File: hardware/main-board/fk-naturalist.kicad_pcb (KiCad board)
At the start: 2 copper layers, 103 x 37.5 mm, 124 parts, among them J1 RF-SMA-EDGE, J10 S2B-PH-SM4-TB, J11 RF-SMA-EDGE, J12 Conn_01x02, J13 CONN_01x06, J14 Conn_01x02, J2 Conn_01x02, J3 S2B-PH-SM4-TB, J4 Conn_01x01, J5 CONN_01x03_SERIAL, J6 Conn_01x05, J7 CONN_02x05_SWD, J8 CONN_01x02, J9 MICRO-USB, M10 FIDUCIAL, M11 FIDUCIAL, M2 FIDUCIAL, M5 FIDUCIAL, M7 MICROSD, M8 FIDUCIAL, M9 FIDUCIAL, Q1 2N7002LT1G, SW1 SPNO, SW2 SPNO, U1 ATWINC1500-MR210PA, U10 FGPMMOPA6H, U11 MAX1704XX, U12 TPS2052B, U13 SK6812, U14 MCP1700T-3302E/MB, U2 ATSAMD21G18A-AU, U3 RFM95W, U4 24AA02E64, U5 S25FL116K0XMFI041, U6 BQ24074RGTT, U7 PCF8523, U8 TL5209, U9 TL5209, Y1 FC-135, Y2 FC-135

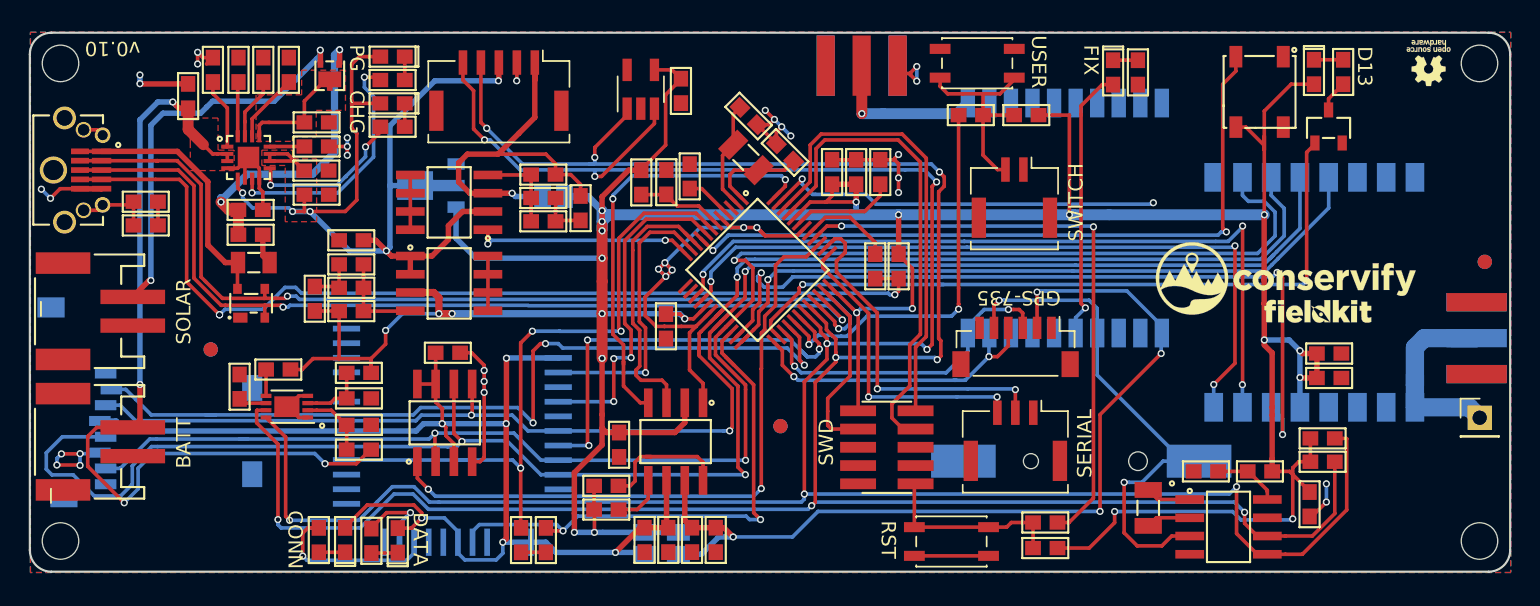
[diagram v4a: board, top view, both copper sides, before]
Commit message: Add new 9 pin sensor connector.
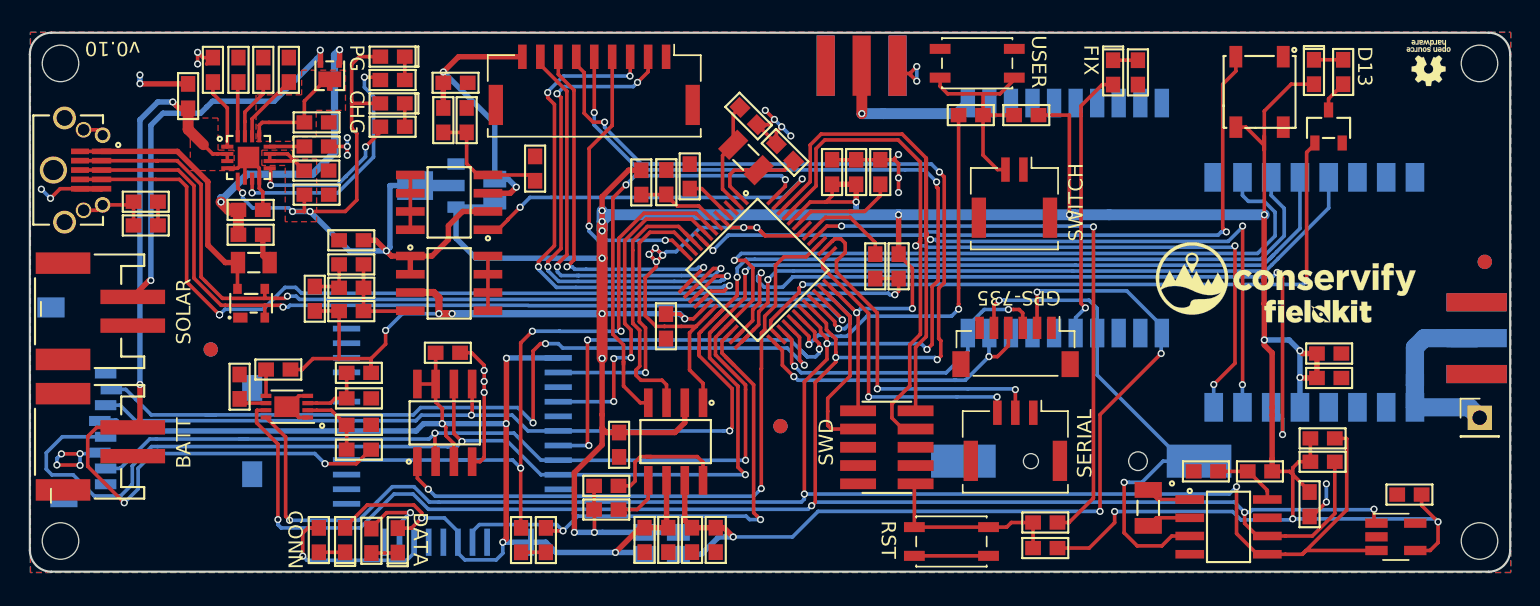
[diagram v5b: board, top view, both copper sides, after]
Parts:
- J6: value Conn_01x05 -> CONN_01x09; footprint conservify:Molex_CLIK-Mate_502382-0570_1x05_P1.25mm_Vertical -> conservify:Molex_CLIK-Mate_502382-0970_1x09_P1.25mm_Vertical
- moved U4 61.1 mm to (169.0, 144.1), turned to 0 degrees
- moved C11 57.9 mm to (170.0, 141.1), turned to 180 degrees
- moved C30 12.3 mm to (103.6, 112.5), turned to 0 degrees
- moved R13 7.92 mm to (102.8, 115.1), turned to 270 degrees
- moved C29 7.60 mm to (104.4, 115.1), turned to 90 degrees
- moved J6 6.65 mm to (113.3, 112.6)
- moved J14 4.11 mm to (106.3, 120.0), turned to 270 degrees
- moved R14 3.71 mm to (109.2, 118.5), turned to 90 degrees
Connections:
- J6 pad 1: /MODULE_3V3 -> GND
- J6 pad 2: GND -> /I2S_BCLK
- J6 pad 3: VBUS -> /I2S_WS
- J6 pad 4: /SCL -> /I2S_DATA
- J7 pad 2: /SWDIO -> /D1_RADIO_D1
- J7 pad 4: /SWCLK -> /D0_RADIO_D2
- U2 pad 12: /D9_MODULE_EN -> /I2S_DATA
- U2 pad 15: /D1_RADIO_D1 -> /I2S_BCLK
- U2 pad 16: /D0_RADIO_D2 -> /I2S_WS
- U2 pad 45: /SWCLK -> /D0_RADIO_D2
- U2 pad 46: /SWDIO -> /D1_RADIO_D1
- U2 pad 47: /A5 -> /D9_MODULE_EN
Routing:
- net /I2S_WS: track 0.00 -> 36.9 mm, vias 0 -> 4
- net /I2S_BCLK: track 0.00 -> 36.6 mm, vias 0 -> 4
- net /SWCLK: track 34.0 -> 0.00 mm
- net /SWDIO: track 32.1 -> 0.00 mm
- net /SCL2: track 0.00 -> 30.6 mm, vias 0 -> 2
- net /A5: track 27.7 -> 0.00 mm, vias 2 -> 0
- net /SDA2: track 0.00 -> 26.7 mm, vias 0 -> 2
- net /I2S_DATA: track 0.00 -> 20.2 mm, vias 0 -> 2
- net /D1_RADIO_D1: track 53.4 -> 73.1 mm
- net /D0_RADIO_D2: track 51.4 -> 68.9 mm
- net VBUS: track 74.1 -> 59.8 mm, vias 5 -> 4
- net /D9_MODULE_EN: track 15.2 -> 25.7 mm
- net /SDA: track 173.3 -> 163.0 mm, vias 8 -> 7
- net 3V3: track 275.5 -> 281.6 mm, vias 23 -> 24
- net /MODULE_3V3: track 27.1 -> 22.0 mm, vias 1 -> 2
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
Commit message: Use more compatible FP for flash.
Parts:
- U5: footprint conservify:SOIC-8-N -> conservify:SOIC-8-N-WIDE
- moved C18 1.10 mm to (103.1, 130.2)
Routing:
- net /D26_FLASH_CS: track 45.5 -> 47.5 mm
- net GND: track 129.9 -> 131.0 mm
- net /PERIPH_3V3: track 89.5 -> 90.1 mm

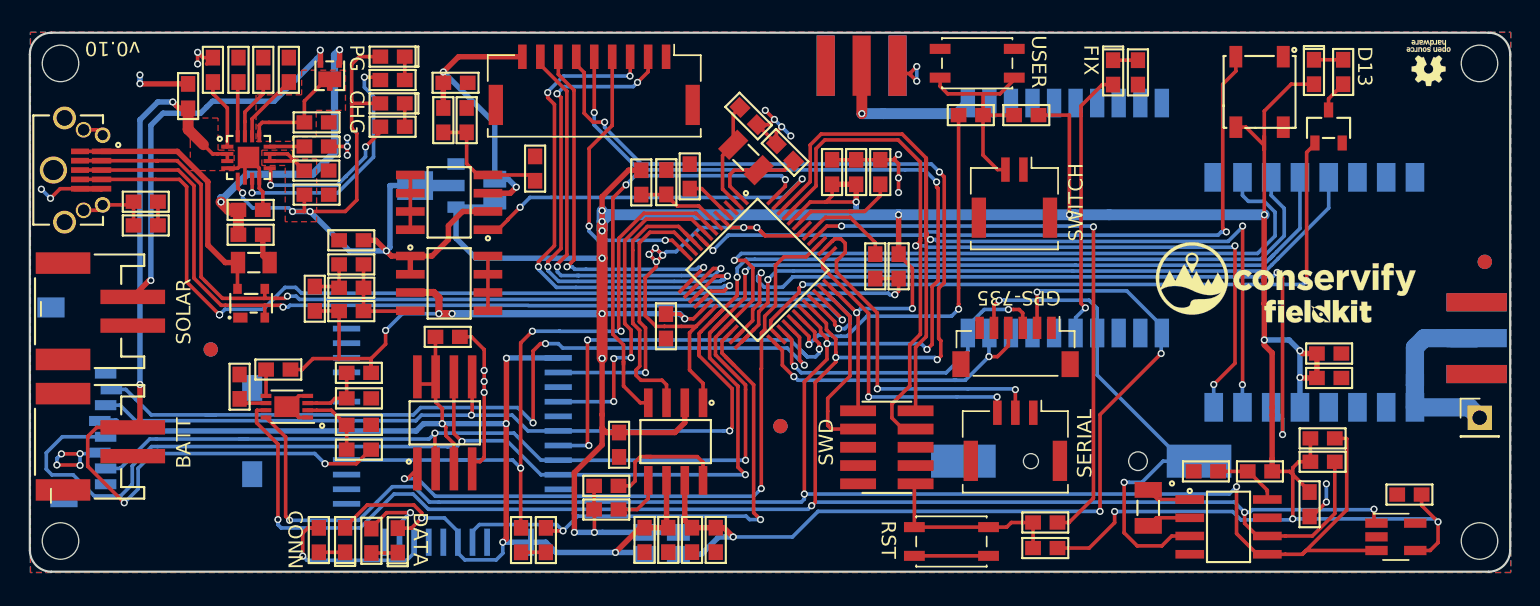
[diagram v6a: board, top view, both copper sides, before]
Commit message: Add some bypass caps on GPS 3v3, see if fix issues are power related.
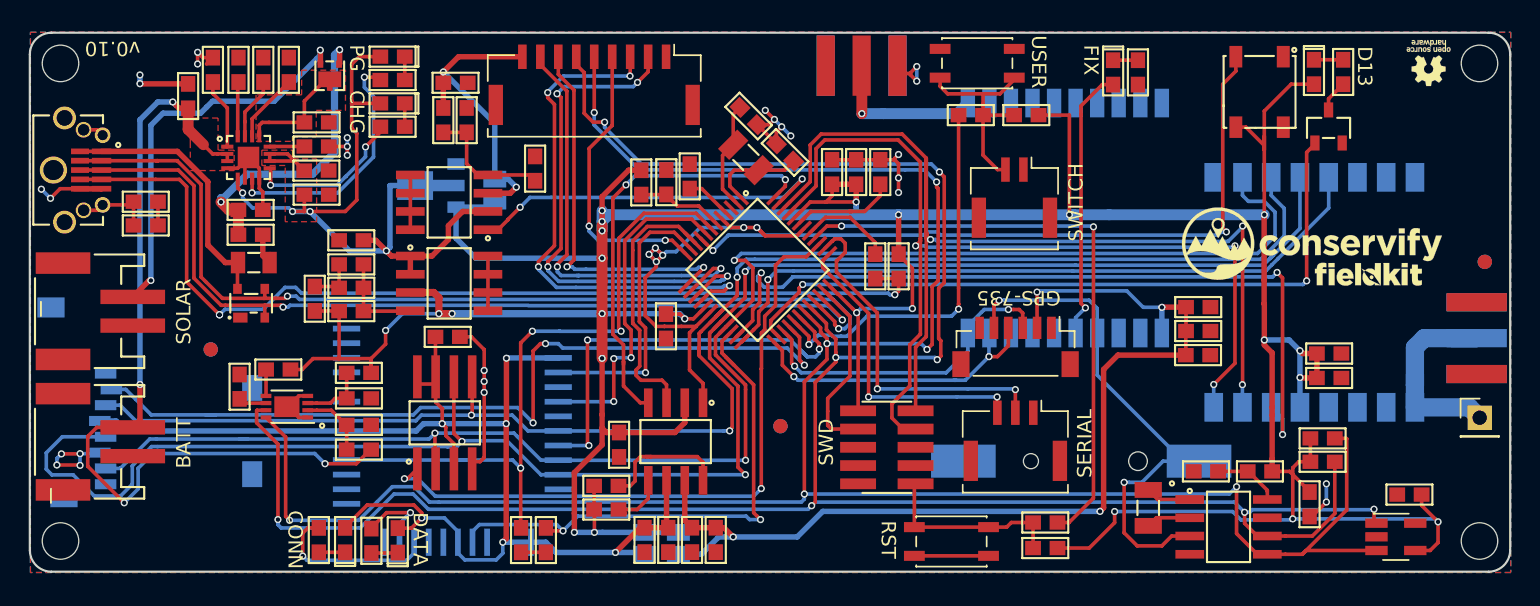
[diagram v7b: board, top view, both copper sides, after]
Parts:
- added C31: 10uF, conservify:CAP-0603, F.Cu at (155.3, 128.1)
- added C32: 47uF, conservify:CAP-0603, F.Cu at (155.3, 131.4)
- added C35: 100nF, conservify:CAP-0603, F.Cu at (155.3, 129.8)
- J12, J14, J2: value Conn_01x02 -> CONN_01x02
- M7: value MICROSD -> MICRO-SD
- moved G*** 4.36 mm to (167.1, 125.8)
- moved G*** 3.03 mm to (163.2, 123.7)
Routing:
- net /GPS_3V3: track 64.3 -> 76.7 mm
